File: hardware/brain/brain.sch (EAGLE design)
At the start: 11 parts, among them IC1 LD117AS33TR, IC2 ESP12

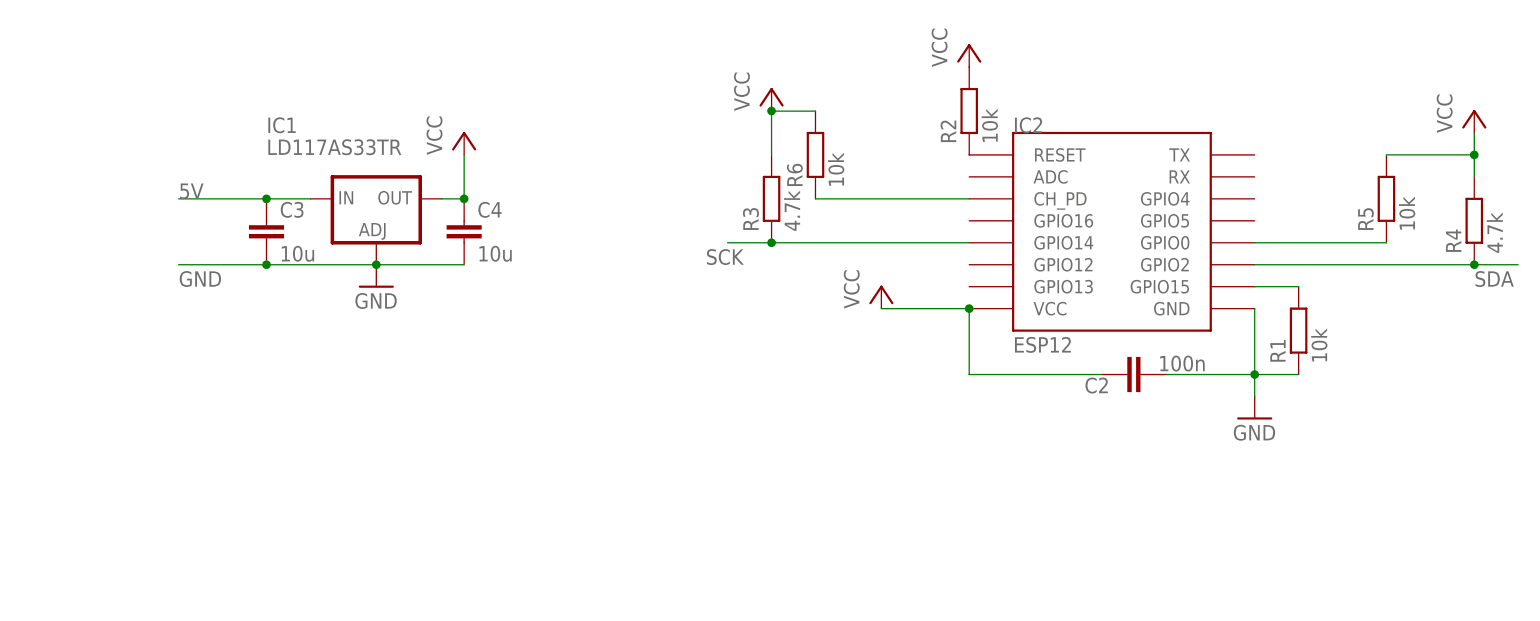
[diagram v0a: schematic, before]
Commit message: add rtc
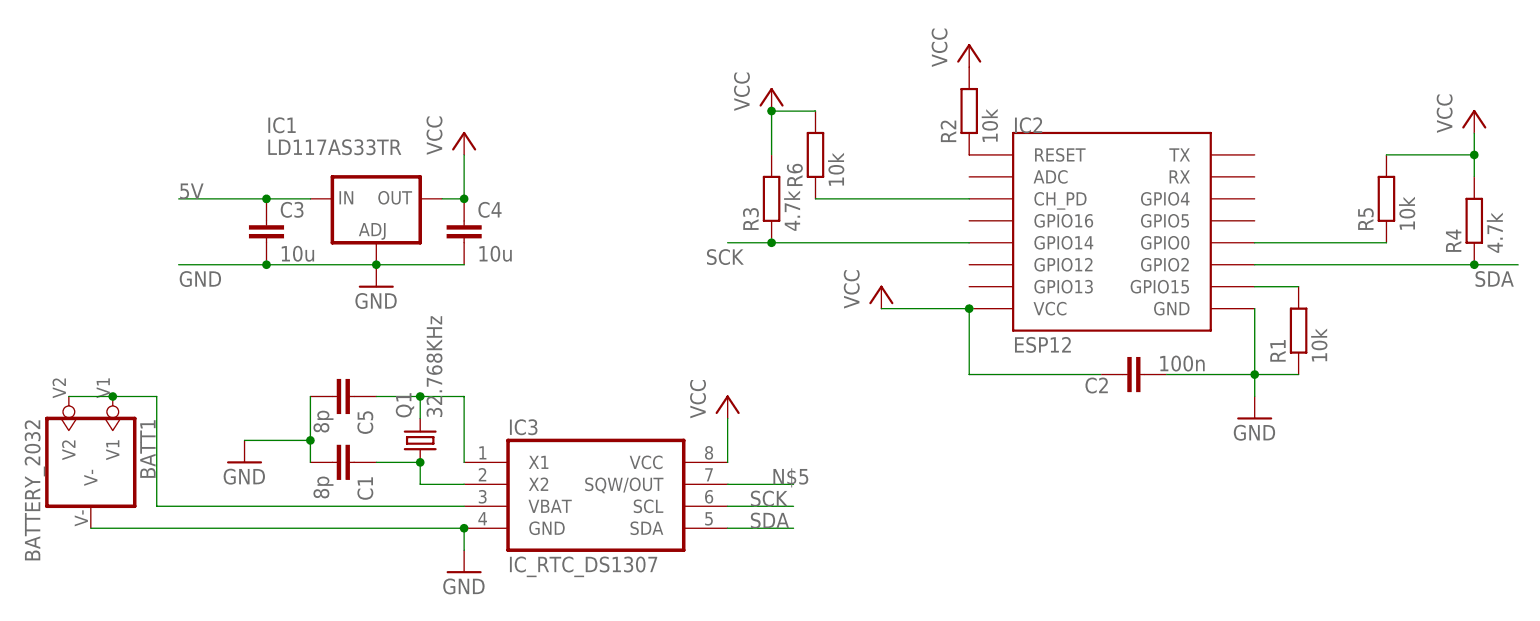
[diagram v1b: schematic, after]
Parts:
- added BATT1: BATTERY_2032, dp_devices:BATTERY_2032
- added C1, C5: 8p, rcl:C-EUC0805
- added IC3: IC_RTC_DS1307, dp_devices:IC_RTC_DS1307
- added Q1: 32.768KHz, crystal:CRYSTALTC26H
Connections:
- new net N$5: IC3.SQW/OUT
- new net N$6: C5.1, IC3.X1, Q1.2
- new net N$7: BATT1.V1, BATT1.V2, IC3.VBAT
- new net N$8: C1.1, IC3.X2, Q1.1
- net GND: now also BATT1.V-, C1.2, C5.2, IC3.GND
- net SCK: now also IC3.SCL
- net SDA: now also IC3.SDA
- net VCC: now also IC3.VCC
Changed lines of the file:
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@@
 <layer number="48" name="Document" color="7" fill="1" visible="no" active="no"/>
 <layer number="49" name="Reference" color="7" fill="1" visible="no" active="no"/>
+<layer number="50" name="dxf" color="7" fill="1" visible="no" active="no"/>
 <layer number="51" name="tDocu" color="7" fill="1" visible="no" active="no"/>
 <layer number="52" name="bDocu" color="7" fill="1" visible="no" active="no"/>
+<layer number="53" name="tGND_GNDA" color="7" fill="1" visible="no" active="no"/>
+<layer number="54" name="bGND_GNDA" color="7" fill="1" visible="no" active="no"/>
+<layer number="56" name="wert" color="7" fill="1" visible="no" active="no"/>
 <layer number="90" name="Modules" color="5" fill="1" visible="yes" active="yes"/>
 <layer number="91" name="Nets" color="2" fill="1" visible="yes" active="yes"/>
@@
 <layer number="97" name="Info" color="7" fill="1" visible="yes" active="yes"/>
 <layer number="98" name="Guide" color="6" fill="1" visible="yes" active="yes"/>
+<layer number="100" name="Muster" color="7" fill="1" visible="yes" active="yes"/>
+<layer number="101" name="Patch_Top" color="7" fill="1" visible="yes" active="yes"/>
+<layer number="102" name="Vscore" color="7" fill="1" visible="yes" active="yes"/>
+<layer number="103" name="ATT_MISO" color="7" fill="1" visible="yes" active="yes"/>
+<layer number="104" name="Name" color="7" fill="1" visible="yes" active="yes"/>
+<layer number="105" name="Beschreib" color="7" fill="1" visible="yes" active="yes"/>
+<layer number="106" name="BGA-Top" color="7" fill="1" visible="yes" active="yes"/>
+<layer number="107" name="BD-Top" color="7" fill="1" visible="yes" active="yes"/>
+<layer number="108" name="centerline" color="7" fill="1" visible="yes" active="yes"/>
+<layer number="116" name="Patch_BOT" color="7" fill="1" visible="yes" active="yes"/>
+<layer number="121" name="_tsilk" color="7" fill="1" visible="yes" active="yes"/>
+<layer number="122" name="_bsilk" color="7" fill="1" visible="yes" active="yes"/>
+<layer number="131" name="prix" color="7" fill="1" visible="yes" active="yes"/>
+<layer number="132" name="test" color="7" fill="1" visible="yes" active="yes"/>
+<layer number="151" name="HeatSink" color="7" fill="1" visible="yes" active="yes"/>
+<layer number="200" name="200bmp" color="7" fill="1" visible="yes" active="yes"/>
+<layer number="201" name="201bmp" color="7" fill="1" visible="yes" active="yes"/>
+<layer number="202" name="202bmp" color="7" fill="1" visible="yes" active="yes"/>
+<layer number="203" name="203bmp" color="7" fill="1" visible="yes" active="yes"/>
+<layer number="204" name="204bmp" color="7" fill="1" visible="yes" active="yes"/>
+<layer number="205" name="205bmp" color="7" fill="1" visible="yes" active="yes"/>
+<layer number="206" name="206bmp" color="7" fill="1" visible="yes" active="yes"/>
+<layer number="207" name="207bmp" color="7" fill="1" visible="yes" active="yes"/>
+<layer number="208" name="208bmp" color="7" fill="1" visible="yes" active="yes"/>
+<layer number="250" name="Descript" color="7" fill="1" visible="yes" active="yes"/>
+<layer number="251" name="SMDround" color="7" fill="1" visible="yes" active="yes"/>
+<layer number="254" name="cooling" color="7" fill="1" visible="yes" active="yes"/>
 </layers>
 <schematic xreflabel="%F%N/%S.%C%R" xrefpart="/%S.%C%R">
@@
 <part name="R6" library="rcl" deviceset="R-EU_" device="R0805" value="10k"/>
 <part name="P+5" library="supply1" deviceset="VCC" device=""/>
+<part name="IC3" library="dp_devices" deviceset="IC_RTC_DS1307" device=""/>
+<part name="P+6" library="supply1" deviceset="VCC" device=""/>
+<part name="GND2" library="supply1" deviceset="GND" device=""/>
+<part name="Q1" library="crystal" deviceset="CRYSTAL" device="TC26H" value="32.768KHz"/>
+<part name="C1" library="rcl" deviceset="C-EU" device="C0805" value="8p"/>
+<part name="C5" library="rcl" deviceset="C-EU" device="C0805" value="8p"/>
+<part name="BATT1" library="dp_devices" deviceset="BATTERY_2032" device=""/>
+<part name="GND4" library="supply1" deviceset="GND" device=""/>
 </parts>
 <sheets>
@@
 <instance part="R6" gate="G$1" x="2.54" y="43.18" rot="R90"/>
 <instance part="P+5" gate="VCC" x="20.32" y="55.88"/>
+<instance part="IC3" gate="G$1" x="-22.86" y="2.54"/>
+<instance part="P+6" gate="VCC" x="-7.62" y="15.24"/>
+<instance part="GND2" gate="1" x="-38.1" y="-5.08" smashed="yes">
+<attribute name="VALUE" x="-40.64" y="-7.62" size="1.778" layer="96"/>
+</instance>
+<instance part="Q1" gate="G$1" x="-43.18" y="10.16" rot="R90"/>
+<instance part="C1" gate="G$1" x="-50.8" y="7.62" rot="R270"/>
+<instance part="C5" gate="G$1" x="-50.8" y="15.24" rot="R270"/>
+<instance part="BATT1" gate="BATT" x="-81.28" y="7.62" rot="R270"/>
+<instance part="GND4" gate="1" x="-63.5" y="7.62" smashed="yes">
+<attribute name="VALUE" x="-66.04" y="5.08" size="1.778" layer="96"/>
+</instance>
 </instances>
 <busses>
@@
 <label x="-71.12" y="27.94" size="1.778" layer="95"/>
 </segment>
+<segment>
+<pinref part="IC3" gate="G$1" pin="GND"/>
+<pinref part="GND2" gate="1" pin="GND"/>
+<wire x1="-38.1" y1="0" x2="-38.1" y2="-2.54" width="0.1524" layer="91"/>
+<pinref part="BATT1" gate="BATT" pin="V-"/>
+<wire x1="-81.28" y1="0" x2="-38.1" y2="0" width="0.1524" layer="91"/>
+<junction x="-38.1" y="0"/>
+</segment>
+<segment>
+<pinref part="C5" gate="G$1" pin="2"/>
+<pinref part="C1" gate="G$1" pin="2"/>
+<wire x1="-55.88" y1="15.24" x2="-55.88" y2="10.16" width="0.1524" layer="91"/>
+<pinref part="GND4" gate="1" pin="GND"/>
+<wire x1="-55.88" y1="10.16" x2="-55.88" y2="7.62" width="0.1524" layer="91"/>
+<wire x1="-63.5" y1="10.16" x2="-55.88" y2="10.16" width="0.1524" layer="91"/>
+<junction x="-55.88" y="10.16"/>
+</segment>
 </net>
 <net name="SDA" class="0">
@@
 <junction x="78.74" y="30.48"/>
 </segment>
+<segment>
+<pinref part="IC3" gate="G$1" pin="SDA"/>
+<wire x1="-7.62" y1="0" x2="0" y2="0" width="0.1524" layer="91"/>
+<label x="-5.08" y="0" size="1.778" layer="95"/>
+</segment>
 </net>
 <net name="SCK" class="0">
@@
 <wire x1="-2.54" y1="33.02" x2="-7.62" y2="33.02" width="0.1524" layer="91"/>
 <junction x="-2.54" y="33.02"/>
+</segment>
+<segment>
+<pinref part="IC3" gate="G$1" pin="SCL"/>
+<wire x1="-7.62" y1="2.54" x2="0" y2="2.54" width="0.1524" layer="91"/>
+<label x="-5.08" y="2.54" size="1.778" layer="95"/>
 </segment>
 </net>
@@
 <junction x="20.32" y="25.4"/>
 </segment>
+<segment>
+<pinref part="IC3" gate="G$1" pin="VCC"/>
+<pinref part="P+6" gate="VCC" pin="VCC"/>
+<wire x1="-7.62" y1="7.62" x2="-7.62" y2="12.7" width="0.1524" layer="91"/>
+</segment>
 </net>
 <net name="N$4" class="0">
@@
 </segment>
 </net>
+<net name="N$7" class="0">
+<segment>
+<pinref part="BATT1" gate="BATT" pin="V2"/>
+<pinref part="BATT1" gate="BATT" pin="V1"/>
+<wire x1="-83.82" y1="15.24" x2="-78.74" y2="15.24" width="0.1524" layer="91"/>
+<wire x1="-78.74" y1="15.24" x2="-73.66" y2="15.24" width="0.1524" layer="91"/>
+<junction x="-78.74" y="15.24"/>
+<pinref part="IC3" gate="G$1" pin="VBAT"/>
+<wire x1="-73.66" y1="15.24" x2="-73.66" y2="2.54" width="0.1524" layer="91"/>
+<wire x1="-73.66" y1="2.54" x2="-38.1" y2="2.54" width="0.1524" layer="91"/>
+</segment>
+</net>
+<net name="N$6" class="0">
+<segment>
+<pinref part="Q1" gate="G$1" pin="2"/>
+<wire x1="-43.18" y1="12.7" x2="-43.18" y2="15.24" width="0.1524" layer="91"/>
+<wire x1="-43.18" y1="15.24" x2="-38.1" y2="15.24" width="0.1524" layer="91"/>
+<pinref part="IC3" gate="G$1" pin="X1"/>
+<wire x1="-38.1" y1="15.24" x2="-38.1" y2="7.62" width="0.1524" layer="91"/>
+<pinref part="C5" gate="G$1" pin="1"/>
+<wire x1="-48.26" y1="15.24" x2="-43.18" y2="15.24" width="0.1524" layer="91"/>
+<junction x="-43.18" y="15.24"/>
+</segment>
+</net>
+<net name="N$8" class="0">
+<segment>
+<pinref part="C1" gate="G$1" pin="1"/>
+<pinref part="Q1" gate="G$1" pin="1"/>
+<wire x1="-48.26" y1="7.62" x2="-43.18" y2="7.62" width="0.1524" layer="91"/>
+<pinref part="IC3" gate="G$1" pin="X2"/>
+<wire x1="-43.18" y1="7.62" x2="-43.18" y2="5.08" width="0.1524" layer="91"/>
+<wire x1="-43.18" y1="5.08" x2="-38.1" y2="5.08" width="0.1524" layer="91"/>
+<junction x="-43.18" y="7.62"/>
+</segment>
+</net>
+<net name="N$5" class="0">
+<segment>
+<pinref part="IC3" gate="G$1" pin="SQW/OUT"/>
+<wire x1="-7.62" y1="5.08" x2="0" y2="5.08" width="0.1524" layer="91"/>
+<label x="-2.54" y="5.08" size="1.778" layer="95"/>
+</segment>
+</net>

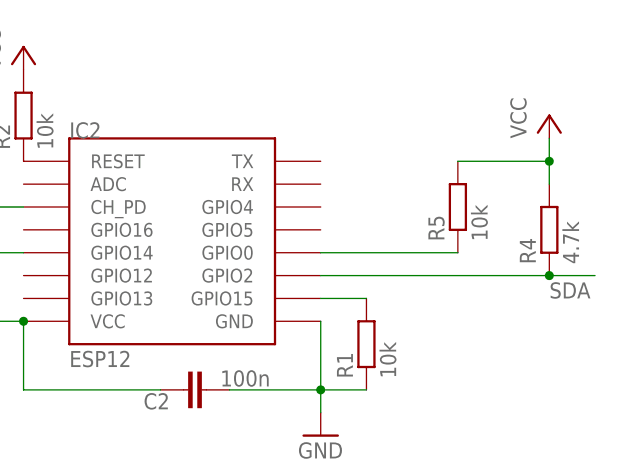
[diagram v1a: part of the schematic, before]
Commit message: edit pin settings, add ch_pd pullup
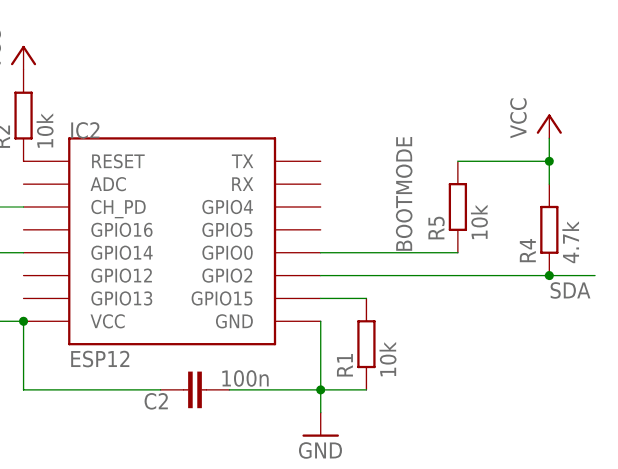
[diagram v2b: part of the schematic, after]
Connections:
- net N$3 renamed BOOTMODE
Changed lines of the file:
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@@
 </segment>
 </net>
-<net name="N$3" class="0">
+<net name="BOOTMODE" class="0">
 <segment>
 <pinref part="IC2" gate="G$1" pin="GPIO0"/>
 <pinref part="R5" gate="G$1" pin="1"/>
 <wire x1="53.34" y1="33.02" x2="68.58" y2="33.02" width="0.1524" layer="91"/>
+<label x="63.5" y="33.02" size="1.778" layer="95" rot="R90"/>
 </segment>
 </net>
